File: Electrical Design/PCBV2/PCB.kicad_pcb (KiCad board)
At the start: 2 copper layers, 50 x 150 mm, 59 parts, among them J1 Conn_02x03_Odd_Even, J2 10118193-0001LF, M1 Camera_Servo, M2 Release_Servo, Q1 LED_MOS, Q2 CAMERA_MOS, Q3 RELEASE_MOS, Q4 BUZZER_MOS, U1 Adafruit_Cam, U10 ATxmega128A4U-AU, U2 ADP3338AKCZ-5-R7, U3 BNO080, U4 ADP3338AKCZ-3.3-R7, U5 PCF8523T_1_118, U6 MS560702BA03-50, U7 SS495A, U8 Openlog, U9 Adafruit_746

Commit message: New PCB
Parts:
- removed BT1: Battery_Cell, Connectors:MOLEX-1X2
- removed D5: 1N4148W-TP, digikey-footprints:SOD-123
- removed J1: Conn_02x03_Odd_Even, Connectors:2X3
- removed J2: 10118193-0001LF, digikey-footprints:USB_Micro_B_Female_10118193-0001LF
- removed LS1: CSS-95B30-SMT, CSS-95B30-SMT:CUI_CSS-95B30-SMT
- removed MOD1: XBP9B-DMWT-002, digikey-footprints:XBEE_PRO-20_THT
- removed Q1: LED_MOS, digikey-footprints:SOT-23-3
- removed Q2: CAMERA_MOS, digikey-footprints:SOT-23-3
- removed Q3: RELEASE_MOS, digikey-footprints:SOT-23-3
- removed Q4: BUZZER_MOS, digikey-footprints:SOT-23-3
- removed U1: Adafruit_Cam, Connectors:MOLEX-1X3
- removed U2: ADP3338AKCZ-5-R7, ADP3338AKCZ-5-R7:SOT230P700X180-4N
- removed U3: BNO080, BNO080:LGA-28
- removed U4: ADP3338AKCZ-3.3-R7, ADP3338AKCZ-3.3RL7:SOT230P700X180-4N
- removed U5: PCF8523T_1_118, digikey-footprints:SOIC-8_W3.9mm
- removed U6: MS560702BA03-50, MS560702BA03-50:SON125P300X500X100-8N
- removed U8: Openlog, Connectors:1X06
- removed U9: Adafruit_746, Connectors:1X09
- moved C17 128.6 mm to (144.5, 98.8)
- moved C18 117.8 mm to (128.8, 97.8)
- moved D3 91.4 mm to (163.4, 79.4)
- moved D2 85.4 mm to (142.9, 84.2)
- moved C4 82.7 mm to (125.0, 99.7), turned to 0 degrees
- moved R7 82.5 mm to (159.3, 87.1), turned to 0 degrees
- moved D4 81.3 mm to (162.9, 86.9)
- moved C7 78.2 mm to (139.3, 84.4)
- moved U10 76.0 mm to (126.1, 81.4), turned to 0 degrees
- moved D1 75.2 mm to (124.9, 97.6)
- moved L1 74.4 mm to (163.5, 77.6)
- moved C1 71.9 mm to (132.5, 99.7), turned to 0 degrees
- moved C2 70.3 mm to (157.9, 77.5), turned to 0 degrees
- moved C13 66.1 mm to (148.3, 80.0)
- moved C6 63.5 mm to (121.3, 99.8)
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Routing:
- net +3V3: track 426.8 -> 0.00 mm, vias 9 -> 0
- net GND: track 321.5 -> 0.00 mm, vias 37 -> 0
- net +6V: track 258.4 -> 0.00 mm, vias 4 -> 0
- net /Release_Servo: track 226.5 -> 0.00 mm, vias 4 -> 0
- net /PA5-Hall_Effect: track 198.7 -> 0.00 mm, vias 4 -> 0
- net +5V: track 176.6 -> 0.00 mm
- net /Camera_Servo: track 157.4 -> 0.00 mm, vias 8 -> 0
- net /OpenLog_MISO: track 126.5 -> 0.00 mm, vias 6 -> 0
- net /BUZZER_MOS: track 122.1 -> 0.00 mm, vias 13 -> 0
- net /LED_MOS: track 105.3 -> 0.00 mm, vias 2 -> 0
- net Net-(U5-Pad2): track 98.8 -> 0.00 mm, vias 2 -> 0
- net /OpenLog_MOSI: track 93.0 -> 0.00 mm, vias 7 -> 0
- net /OpenLog_GRN: track 91.2 -> 0.00 mm, vias 4 -> 0
- net /MISO: track 88.4 -> 0.00 mm, vias 10 -> 0
- net /MCU_VCC: track 81.2 -> 0.00 mm
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- removed copper zone on B.Cu, net GND
- removed copper zone on F.Cu, net GND
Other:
- board outline removed
- net class Default: clearance 0.1524 -> 0.2; trace_width 0.1524 -> 0.25; via_dia 0.6858 -> 0.8; via_drill 0.3302 -> 0.4
- rule trace_clearance: 0.1524 -> 0.2
- rule trace_min: 0.1524 -> 0.2
- rule via_min_drill: 0.254 -> 0.3
- rule via_min_size: 0.508 -> 0.4

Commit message: fix the libraries
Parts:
- added BT1: Battery_Cell, Connectors:MOLEX-1X2, F.Cu at (154.8, 138.0)
- added D5: 1N4148W-TP, digikey-footprints:SOD-123, F.Cu at (166.6, 113.9)
- added J1: Conn_02x03_Odd_Even, Connectors:2X3, F.Cu at (167.9, 120.7)
- added J2: 10118193-0001LF, digikey-footprints:USB_Micro_B_Female_10118193-0001LF, F.Cu at (175.3, 113.8)
- added LS1: CSS-95B30-SMT, CSS-95B30-SMT:CUI_CSS-95B30-SMT, F.Cu at (153.3, 121.7)
- added MOD1: XBP9B-DMWT-002, digikey-footprints:XBEE_PRO-20_THT, F.Cu at (135.5, 127.3)
- added Q1: LED_MOS, digikey-footprints:SOT-23-3, F.Cu at (165.6, 128.3)
- added Q2: CAMERA_MOS, digikey-footprints:SOT-23-3, F.Cu at (165.3, 124.4)
- added Q3: RELEASE_MOS, digikey-footprints:SOT-23-3, F.Cu at (169.0, 124.4)
- added Q4: BUZZER_MOS, digikey-footprints:SOT-23-3, F.Cu at (176.2, 118.8)
- added U1: Adafruit_Cam, Connectors:MOLEX-1X3, F.Cu at (157.3, 131.1)
- added U2: ADP3338AKCZ-5-R7, ADP3338AKCZ-5-R7:SOT230P700X180-4N, F.Cu at (162.5, 118.9)
- added U3: BNO080, BNO080:LGA-28, F.Cu at (181.8, 113.2)
- added U4: ADP3338AKCZ-3.3-R7, ADP3338AKCZ-3.3RL7:SOT230P700X180-4N, F.Cu at (152.0, 131.4)
- added U5: PCF8523T_1_118, digikey-footprints:SOIC-8_W3.9mm, F.Cu at (150.7, 138.6)
- added U6: MS560702BA03-50, MS560702BA03-50:SON125P300X500X100-8N, F.Cu at (161.4, 125.1)
- added U8: Openlog, Connectors:1X06, F.Cu at (149.4, 114.1)
- added U9: Adafruit_746, Connectors:1X09, F.Cu at (149.4, 111.4)

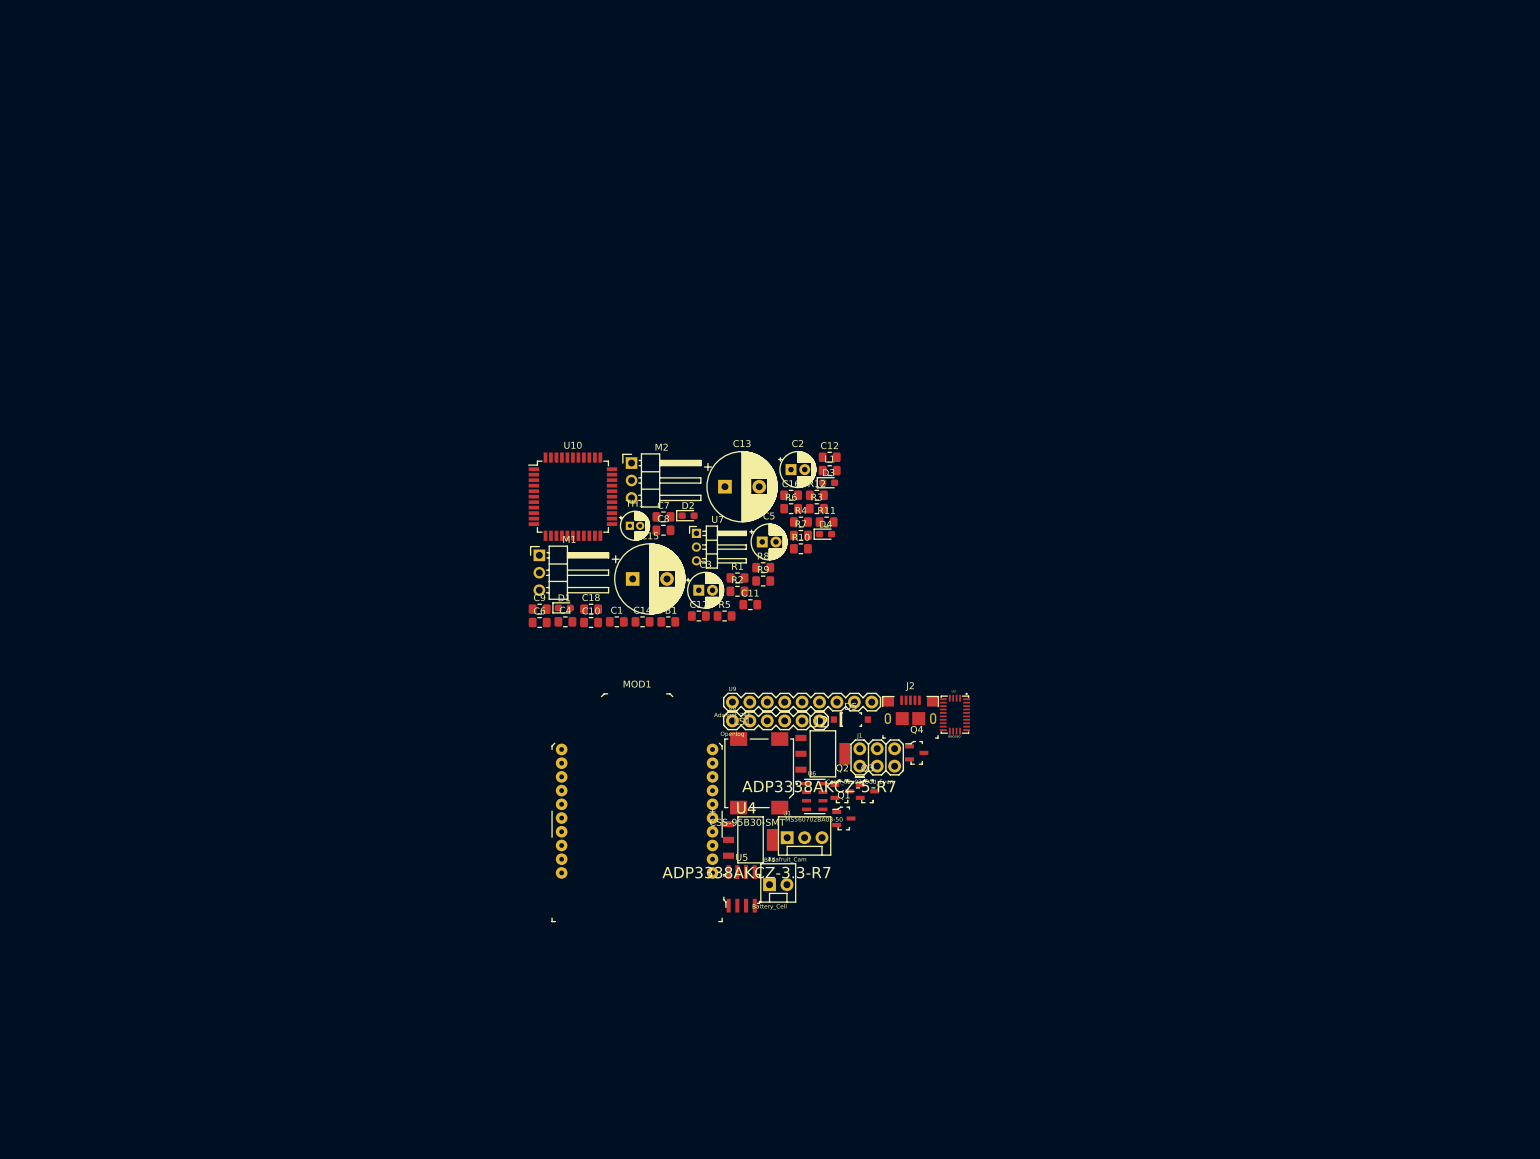
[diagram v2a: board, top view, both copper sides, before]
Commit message: Layout and edge cuts
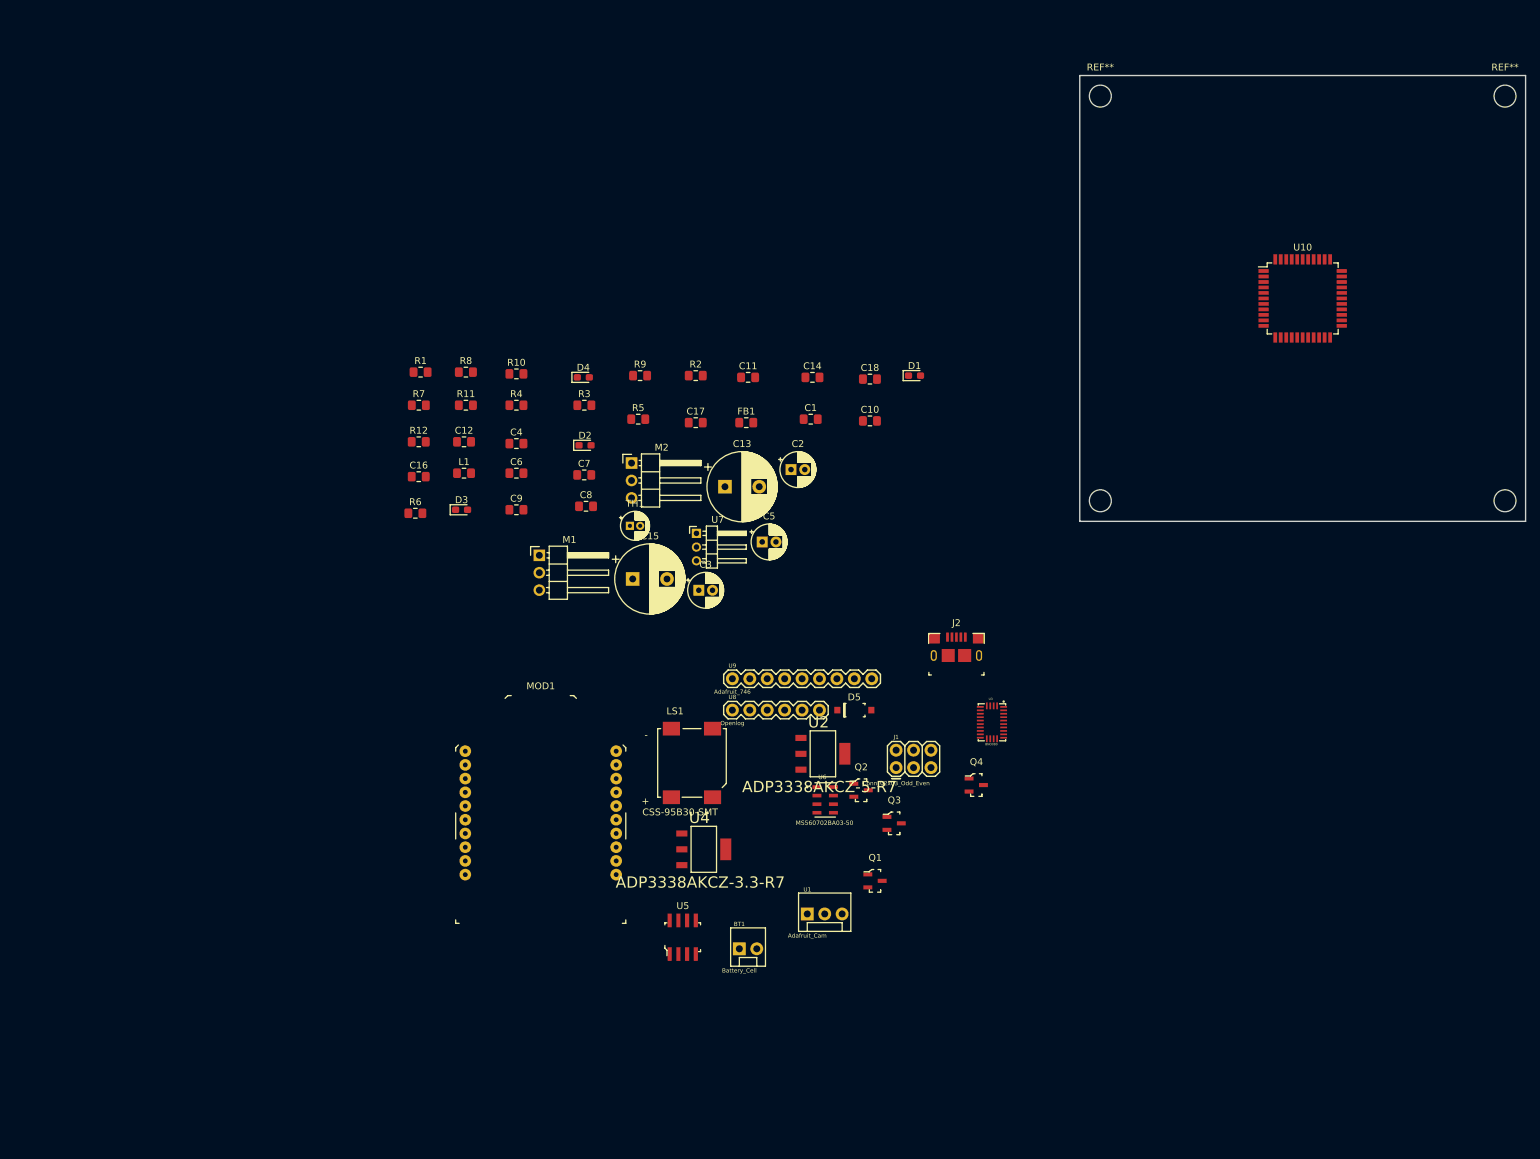
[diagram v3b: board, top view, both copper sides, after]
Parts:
- added REF**: MountingHole_3.2mm_M3, MountingHole:MountingHole_3.2mm_M3, F.Cu at (203.0, 23.0)
- added REF**: MountingHole_3.2mm_M3, MountingHole:MountingHole_3.2mm_M3, F.Cu at (262.0, 23.0)
- added REF**: MountingHole_3.2mm_M3, MountingHole:MountingHole_3.2mm_M3, F.Cu at (262.0, 82.0)
- added REF**: MountingHole_3.2mm_M3, MountingHole:MountingHole_3.2mm_M3, F.Cu at (203.0, 82.0)
- moved U10 110.3 mm to (232.5, 52.5)
- moved D1 61.3 mm to (175.9, 63.8)
- moved R7 58.8 mm to (103.6, 68.1)
- moved R12 58.6 mm to (103.6, 73.4)
- moved R11 55.3 mm to (110.5, 68.1)
- moved R1 55.1 mm to (103.9, 63.2)
- moved R6 54.8 mm to (103.1, 83.8)
- moved C16 54.4 mm to (103.6, 78.5)
- moved D3 53.7 mm to (109.9, 83.3)
- moved C12 53.4 mm to (110.2, 73.4)
- moved L1 53.3 mm to (110.2, 78.0)
- moved C18 52.7 mm to (169.4, 64.3)
- moved R8 51.9 mm to (110.5, 63.2)
- moved C10 50.2 mm to (169.4, 70.4)
- moved R10 48.7 mm to (117.9, 63.5)
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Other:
- board outline added: 65 x 65 mm

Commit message: major revision progress
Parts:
- removed C17, C18: 100nF, Capacitor_SMD:C_0805_2012Metric_Pad1.15x1.40mm_HandSolder
- removed D3: 5V Status, LED_SMD:LED_0603_1608Metric_Pad1.05x0.95mm_HandSolder
- removed REF** (x4): MountingHole_3.2mm_M3, MountingHole:MountingHole_3.2mm_M3
- removed U10: ATxmega128A4U-AU, Package_QFP:TQFP-44_10x10mm_P0.8mm
- added H1: MountingHole, MountingHole:MountingHole_3.2mm_M3, F.Cu at (203.0, 23.0)
- added H2: MountingHole, MountingHole:MountingHole_3.2mm_M3, F.Cu at (203.0, 97.0)
- added H3: MountingHole, MountingHole:MountingHole_3.2mm_M3, F.Cu at (262.0, 23.0)
- added H4: MountingHole, MountingHole:MountingHole_3.2mm_M3, F.Cu at (262.0, 97.0)
- added Q5: CAMERA_MOS, digikey-footprints:SOT-23-3, B.Cu at (222.2, 90.4)
- added R13: 10K, Resistor_SMD:R_0805_2012Metric_Pad1.15x1.40mm_HandSolder, B.Cu at (221.0, 86.6)
- BT1: footprint Connectors:MOLEX-1X2 -> Connectors:MOLEX-1X2_LOCK
- C1, C4: value 1uF -> 0.1uF
- C10: value 47pF -> 100nF
- C11: value 1uF -> 10uF
- C13: footprint Capacitor_THT:CP_Radial_D10.0mm_P5.00mm -> Capacitor_SMD:C_0805_2012Metric_Pad1.15x1.40mm_HandSolder
- C15: value 10uF -> 100nF; footprint Capacitor_THT:CP_Radial_D10.0mm_P5.00mm -> Capacitor_SMD:C_0805_2012Metric_Pad1.15x1.40mm_HandSolder
- C2: footprint Capacitor_THT:CP_Radial_D5.0mm_P2.00mm -> Capacitor_SMD:C_0805_2012Metric_Pad1.15x1.40mm_HandSolder
- C3: value 0.1uF -> 1uF; footprint Capacitor_THT:CP_Radial_D5.0mm_P2.00mm -> Capacitor_SMD:C_0805_2012Metric_Pad1.15x1.40mm_HandSolder; moved to B.Cu
- C5: value 0.1uF -> 1uF; footprint Capacitor_THT:CP_Radial_D5.0mm_P2.00mm -> Capacitor_SMD:C_0805_2012Metric_Pad1.15x1.40mm_HandSolder
- C6: value 1uF -> 0.1uf
- C8: value 0.1uf -> 47pF
- FB1, LS1, MOD1, Q1, Q3, R7, R8, R9: moved to B.Cu
- J1: value Conn_02x03_Odd_Even -> PDI_Interface
- M1: value Camera_Servo -> Finn_servo; footprint Connector_PinHeader_2.54mm:PinHeader_1x03_P2.54mm_Horizontal -> Connectors:MOLEX-1X3_LOCK
- M2: footprint Connector_PinHeader_2.54mm:PinHeader_1x03_P2.54mm_Horizontal -> Connectors:MOLEX-1X3_LOCK
- Q2: value CAMERA_MOS -> FINN_MOS; moved to B.Cu
- U1: footprint Connectors:MOLEX-1X3 -> Connectors:MOLEX-1X3_LOCK
- U2: value ADP3338AKCZ-5-R7 -> BNO080; footprint ADP3338AKCZ-5-R7:SOT230P700X180-4N -> BNO080:LGA-28
- U3: value BNO080 -> 6->3V3; footprint BNO080:LGA-28 -> ADP3338AKCZ-3.3RL7:SOT230P700X180-4N; moved to B.Cu
- U4: value ADP3338AKCZ-3.3-R7 -> RTC; footprint ADP3338AKCZ-3.3RL7:SOT230P700X180-4N -> digikey-footprints:SOIC-8_W3.9mm
- U5: value PCF8523T_1_118 -> MS560702BA03-50; footprint digikey-footprints:SOIC-8_W3.9mm -> MS560702BA03-50:SON125P300X500X100-8N
- U6: value MS560702BA03-50 -> SS49E; footprint MS560702BA03-50:SON125P300X500X100-8N -> Connectors:MOLEX-1X3_LOCK
- U7: value SS495A -> Openlog; footprint Connector_PinHeader_2.00mm:PinHeader_1x03_P2.00mm_Horizontal -> Connectors:1X06
- U8: value Openlog -> Adafruit_746; footprint Connectors:1X06 -> Connectors:1X09
- U9: value Adafruit_746 -> ATxmega128A4U-AU; footprint Connectors:1X09 -> Package_QFP:TQFP-44_10x10mm_P0.8mm
- moved R7 155.5 mm to (259.1, 70.1), turned to 270 degrees
- moved MOD1 147.3 mm to (232.9, 31.2), turned to 180 degrees
- moved L1 143.3 mm to (253.5, 77.1), turned to 180 degrees
- moved U5 142.0 mm to (231.8, 35.5)
- moved C16 139.7 mm to (241.9, 58.8), turned to 270 degrees
- moved D4 134.3 mm to (261.2, 77.5), turned to 180 degrees
- moved D2 133.6 mm to (261.2, 81.3), turned to 180 degrees
- moved Q3 129.6 mm to (255.3, 29.0), turned to 90 degrees
- moved R6 127.7 mm to (230.6, 76.5), turned to 270 degrees
- moved M2 126.8 mm to (250.2, 24.3)
- moved C8 126.4 mm to (240.3, 24.6)
- moved C7 125.5 mm to (240.3, 22.6)
- moved R9 124.5 mm to (256.5, 33.0), turned to 90 degrees
- moved J1 123.4 mm to (259.8, 33.0), turned to 270 degrees
- moved C15 120.4 mm to (246.5, 48.3)
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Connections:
- C1 pad 1: GND -> +3V3
- C1 pad 2: +6V -> GND
- C10 pad 1: GND -> +3V3
- C10 pad 2: +3V3 -> GND
- C11 pad 1: GND -> /MCU_VCC
- C11 pad 2: +5V -> GND
- C12 pad 1: +3V3 -> /MCU_VCC
- C13 pad 1: /MCU_VCC -> GND
- C13 pad 2: GND -> /MCU_AVCC
- C15 pad 1: /MCU_AVCC -> GND
- C15 pad 2: GND -> /MCU_AVCC
- C3 pad 1: +3V3 -> GND
- C3 pad 2: GND -> +6V
- C4 pad 1: GND -> Net-(C4-Pad1)
- C4 pad 2: +6V -> GND
- C5 pad 1: Net-(C5-Pad1) -> +3V3
- C6 pad 1: +5V -> GND
- C6 pad 2: GND -> Net-(C6-Pad2)
- C7 pad 1: +3V3 -> GND
- C7 pad 2: GND -> +3V3
- C8 pad 2: Net-(C8-Pad2) -> +3V3
- C9 pad 2: +3V3 -> +6V
- M1 pad 1: /Camera_Servo -> /FINN_SERVO
- R5 pad 2: Net-(C8-Pad2) -> Net-(C6-Pad2)
- R8 pad 1: /CAMERA_MOS -> /FINN_MOS
- U1 pad 1: +5V -> +3V3
- U1 pad 3: /CAMERA_DATA -> Net-(Q5-Pad3)
- U2 pad 1: GND -> (no net)
- U2 pad 2: +5V -> GND
- U2 pad 3: +6V -> +3V3
- U2 pad 4: +5V -> /BNO_BOOTN
- U3 pad 1: (no net) -> GND
- U3 pad 2: GND -> +3V3
- U3 pad 3: +3V3 -> +6V
- U3 pad 4: /BNO_BOOTN -> +3V3
- U4 pad 1: GND -> Net-(U4-Pad1)
- U4 pad 2: +3V3 -> Net-(U4-Pad2)
- U4 pad 3: +6V -> Net-(U4-Pad3)
- U4 pad 4: +3V3 -> GND
- U5 pad 1: Net-(U5-Pad1) -> +3V3
- U5 pad 2: Net-(U5-Pad2) -> GND
- U5 pad 3: Net-(U5-Pad3) -> GND
- U5 pad 4: GND -> /~SS_5607
- U5 pad 5: /SDA -> /~SS_5607
- U5 pad 6: /SCL -> /MISO
- U5 pad 7: Net-(R6-Pad2) -> /MOSI
- U5 pad 8: Net-(C8-Pad2) -> /SCLK
- U6 pad 1: +3V3 -> +6V
- U6 pad 3: GND -> /PA5-Hall_Effect
- U7 pad 1: +5V -> GND
- U7 pad 3: /PA5-Hall_Effect -> +3V3
- U8 pad 1: GND -> Net-(U8-Pad1)
- U8 pad 2: GND -> Net-(U8-Pad2)
- U8 pad 3: +3V3 -> Net-(U8-Pad3)
- U8 pad 4: /OpenLog_MISO -> Net-(U8-Pad4)
- U8 pad 5: /OpenLog_MOSI -> /GPS_MISO
- U8 pad 6: /OpenLog_GRN -> /GPS_MOSI
- U9 pad 1: Net-(U9-Pad1) -> /PA5-Hall_Effect
- U9 pad 2: Net-(U9-Pad2) -> /PA6-Therm
- U9 pad 3: Net-(U9-Pad3) -> /PA7-Voltage
- U9 pad 5: /GPS_MISO -> Net-(U9-Pad5)
- U9 pad 6: /GPS_MOSI -> Net-(U9-Pad6)
- U9 pad 7: GND -> Net-(U9-Pad7)
- U9 pad 8: +3V3 -> GND
- U9 pad 9: Net-(U9-Pad9) -> /MCU_VCC
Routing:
- net +6V: track 0.00 -> 36.9 mm, vias 0 -> 2
- net +3V3: track 0.00 -> 28.0 mm, vias 0 -> 1
- net /MCU_VCC: track 0.00 -> 13.2 mm
- net Net-(D1-Pad1): track 0.00 -> 7.63 mm, vias 0 -> 1
- net Net-(Q5-Pad3): track 0.00 -> 4.19 mm
- net Net-(M1-Pad3): track 0.00 -> 4.06 mm
- net Net-(C6-Pad2): track 0.00 -> 4.06 mm
- net Net-(R6-Pad2): track 0.00 -> 4.01 mm
- net Net-(D5-PadA): track 0.00 -> 3.94 mm
- net /PDI_CLK: track 0.00 -> 3.47 mm
- net Net-(Q5-Pad1): track 0.00 -> 1.84 mm
- net Net-(Q2-Pad1): track 0.00 -> 1.84 mm
- net Net-(Q1-Pad1): track 0.00 -> 1.77 mm
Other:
- board size 65 x 65 mm -> 65 x 80 mm
- net class 6V Power added: clearance 0.254, trace_width 0.635, via_dia 0.762, via_drill 0.381
- net class Default: clearance 0.2 -> 0.254; trace_width 0.25 -> 0.254; via_dia 0.8 -> 0.762; via_drill 0.4 -> 0.381
- rule trace_clearance: 0.2 -> 0.254
- rule trace_min: 0.2 -> 0.1524
- rule via_min_drill: 0.3 -> 0.3302
- rule via_min_size: 0.4 -> 0.6858

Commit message: Start tracing
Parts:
- moved FB1 102.8 mm to (149.9, 87.1)
- moved C15 102.4 mm to (148.8, 79.0), turned to 180 degrees
- moved C13 100.5 mm to (148.8, 82.3), turned to 180 degrees
- moved C11 99.8 mm to (157.7, 102.1)
- moved C12 99.8 mm to (128.4, 89.5)
- moved C16 99.8 mm to (146.2, 87.0)
- moved C3 99.8 mm to (154.4, 120.7)
- moved C5 99.8 mm to (157.0, 109.7)
- moved C6 99.8 mm to (130.0, 102.9)
- moved C9 99.8 mm to (112.8, 57.4)
- moved D1 99.8 mm to (165.5, 101.9)
- moved D2 99.8 mm to (165.5, 109.5)
- moved D4 99.8 mm to (165.5, 105.7)
- moved H3 99.8 mm to (166.2, 51.2)
- moved H4 99.8 mm to (166.2, 125.2)
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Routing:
- net +3V3: track 28.0 -> 321.6 mm, vias 1 -> 3
- net +6V: track 36.9 -> 195.4 mm, vias 2 -> 6
- net /MCU_VCC: track 13.2 -> 67.3 mm, vias 0 -> 3
- net /OpenLog_MOSI: track 0.00 -> 44.4 mm, vias 0 -> 4
- net /PDI_DATA: track 0.00 -> 43.8 mm, vias 0 -> 2
- net /OpenLog_GRN: track 0.00 -> 39.9 mm, vias 0 -> 3
- net /PDI_CLK: track 3.47 -> 39.6 mm, vias 0 -> 2
- net /SDA: track 0.00 -> 25.8 mm, vias 0 -> 2
- net /MCU_AVCC: track 0.00 -> 23.1 mm, vias 0 -> 1
- net /SCLK: track 0.00 -> 19.4 mm, vias 0 -> 1
- net /SCL: track 0.00 -> 14.0 mm, vias 0 -> 2
- net /MISO: track 0.00 -> 12.8 mm
- net /MOSI: track 0.00 -> 8.90 mm
- net Net-(Q4-Pad1): track 0.00 -> 5.43 mm
- net Net-(LS1-PadN): track 0.00 -> 4.53 mm, vias 0 -> 1
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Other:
- net class Default: trace_width 0.254 -> 0.2032

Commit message: Finish v02
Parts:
- added G***: LOGO, skyfire_logo:skyfire_logo, B.Cu at (113.5, 54.4)
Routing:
- net GND: track 0.00 -> 179.7 mm, vias 0 -> 21
- net /SCLK: track 19.4 -> 97.6 mm, vias 1 -> 2
- net /~SS_BNO080: track 1.12 -> 76.5 mm, vias 0 -> 2
- net /MISO: track 12.8 -> 80.0 mm, vias 0 -> 4
- net /FINN_MOS: track 0.00 -> 59.2 mm, vias 0 -> 3
- net /OpenLog_MISO: track 0.00 -> 55.3 mm, vias 0 -> 4
- net /PA5-Hall_Effect: track 0.00 -> 51.6 mm, vias 0 -> 2
- net +6V: track 195.4 -> 244.2 mm, vias 6 -> 7
- net /RELEASE_MOS: track 0.00 -> 48.3 mm, vias 0 -> 3
- net /Release_Servo: track 0.00 -> 47.2 mm, vias 0 -> 2
- net /PA6-Therm: track 4.06 -> 50.8 mm, vias 0 -> 2
- net /CAMERA_DATA: track 0.00 -> 46.0 mm, vias 0 -> 3
- net /MOSI: track 8.90 -> 53.2 mm, vias 0 -> 6
- net /~SS_XBEE: track 0.00 -> 42.7 mm, vias 0 -> 6
- net /PA7-Voltage: track 2.29 -> 35.5 mm, vias 0 -> 2
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- added copper zone on B.Cu, net GND
- added copper zone on F.Cu, net GND
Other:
- board text added: "Designed February 2019 UAH Space Hardware Club"
- board text added: "Skyfire v02"

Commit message: change logo stuff
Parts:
- moved G*** 10.9 mm to (116.8, 64.8)
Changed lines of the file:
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@@
   )
   (layers
-    (0 F.Cu signal)
-    (31 B.Cu signal)
+    (0 F.Cu signal hide)
+    (31 B.Cu signal hide)
     (32 B.Adhes user)
     (33 F.Adhes user)
@@
   )
   (module skyfire_logo:skyfire_logo (layer B.Cu)
-    (at 113.538 54.356 90)
+    (at 116.84 64.77 90)
     (fp_text reference G*** (at 0 0 90) (layer B.SilkS) hide
       (effects (font (size 1.524 1.524) (thickness 0.3)) (justify mirror))
@@
       (xy 1.435131 -2.769742) (xy 1.440972 -2.774388)) (layer B.SilkS) (width 0.01))
   )
-  (gr_text "Designed February 2019\nUAH Space Hardware Club" (at 113.792 60.96) (layer B.SilkS)
+  (gr_text "Designed February 2019\nUAH Space Hardware Club" (at 116.84 71.374) (layer B.SilkS)
     (effects (font (size 0.762 0.762) (thickness 0.127)) (justify mirror))
   )
-  (gr_text "Skyfire\nv02" (at 164.338 124.714) (layer F.SilkS)
+  (gr_text "Skyfire\nv02" (at 165.354 118.11) (layer F.SilkS)
     (effects (font (size 1.5 1.5) (thickness 0.3)))
   )
